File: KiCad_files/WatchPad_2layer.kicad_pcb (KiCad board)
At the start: 2 copper layers, 154 x 53.4 mm, 46 parts, among them SW1 SW_Push, SW10 SW_Push, SW11 SW_Push, SW12 SW_Push, SW2 SW_Push, SW3 SW_Push, SW4 SW_Push, SW5 SW_Push, SW6 SW_Push, SW7 SW_Push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

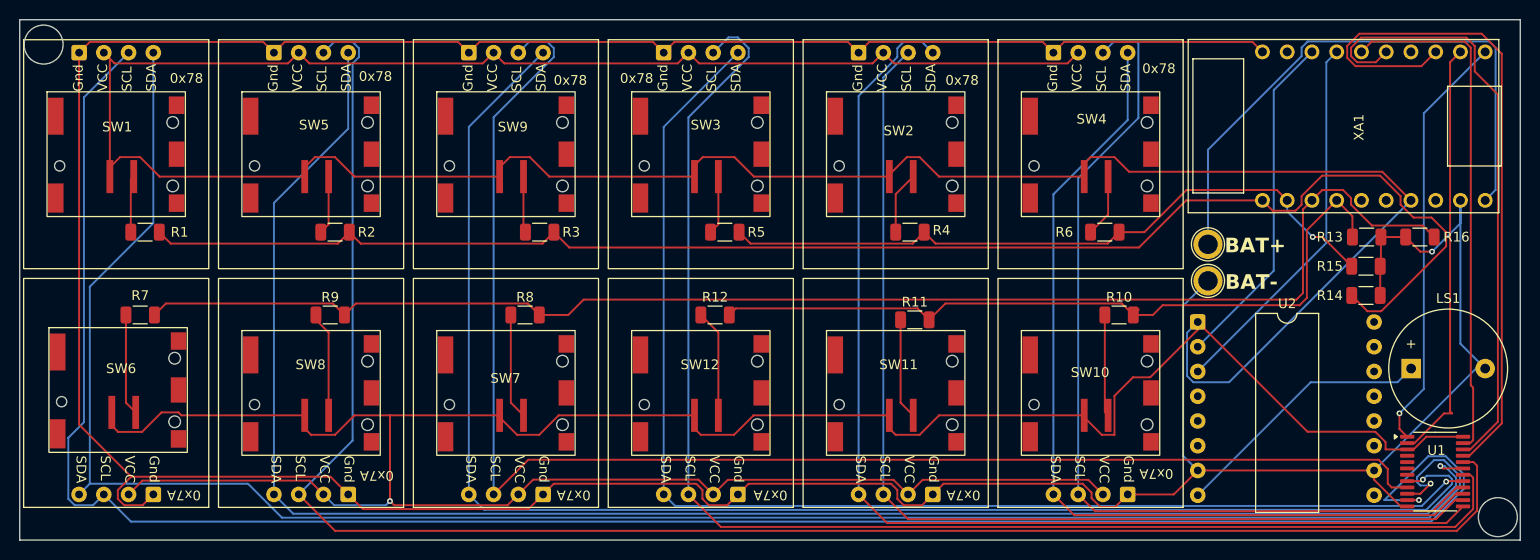
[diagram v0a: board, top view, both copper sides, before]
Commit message: Added BOM and Slightly changed PCB layout
Changed mounting solution for speaker to use more standard 6.5mm hole spacing
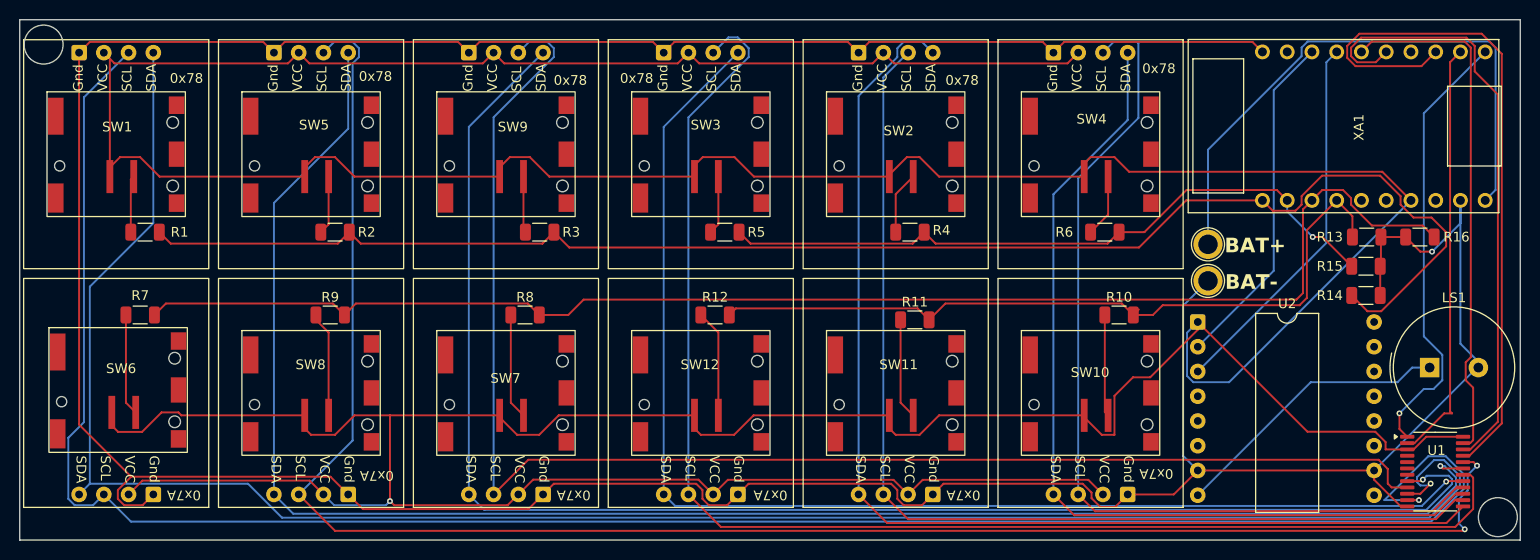
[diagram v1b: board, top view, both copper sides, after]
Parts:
- LS1: footprint Buzzer_Beeper:Buzzer_12x9.5RM7.6 -> Buzzer_Beeper:Buzzer_TDK_PS1240P02BT_D12.2mm_H6.5mm
- moved LS1 1.90 mm to (234.0, 119.4)
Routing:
- net Net-(U1-A0): track 43.5 -> 45.6 mm
- net Net-(U2-SPK_2): track 27.3 -> 28.2 mm
- net Net-(D11-SCL): track 182.3 -> 183.1 mm, vias 0 -> 2
